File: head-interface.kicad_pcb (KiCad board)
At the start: 2 copper layers, 51.1 x 19.6 mm, 10 parts, among them J1 NOZ, J2 FANS, J3 MOTOR_IN, J4 THERM, J5 HEATER, J6 PART_FAN, J7 FAN, J8 MOTOR

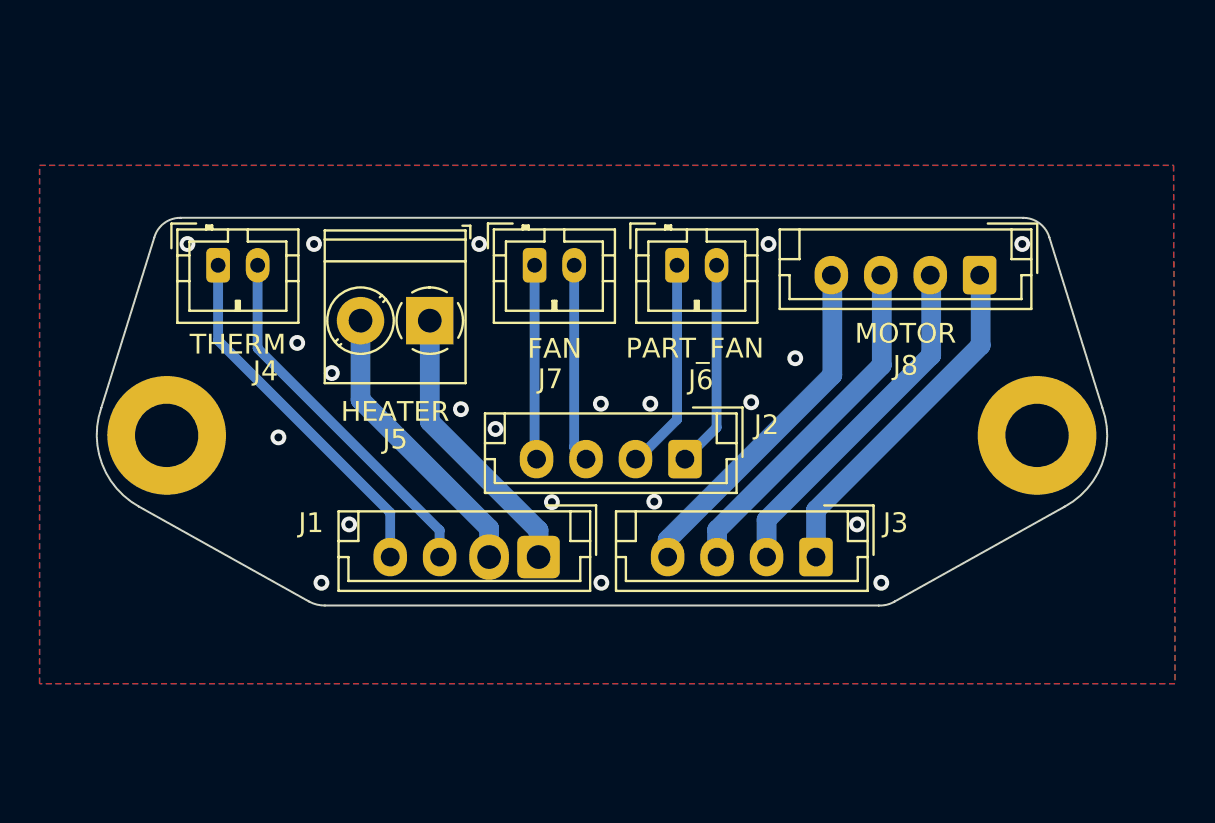
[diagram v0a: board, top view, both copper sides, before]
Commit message: added 2nd part fan connector
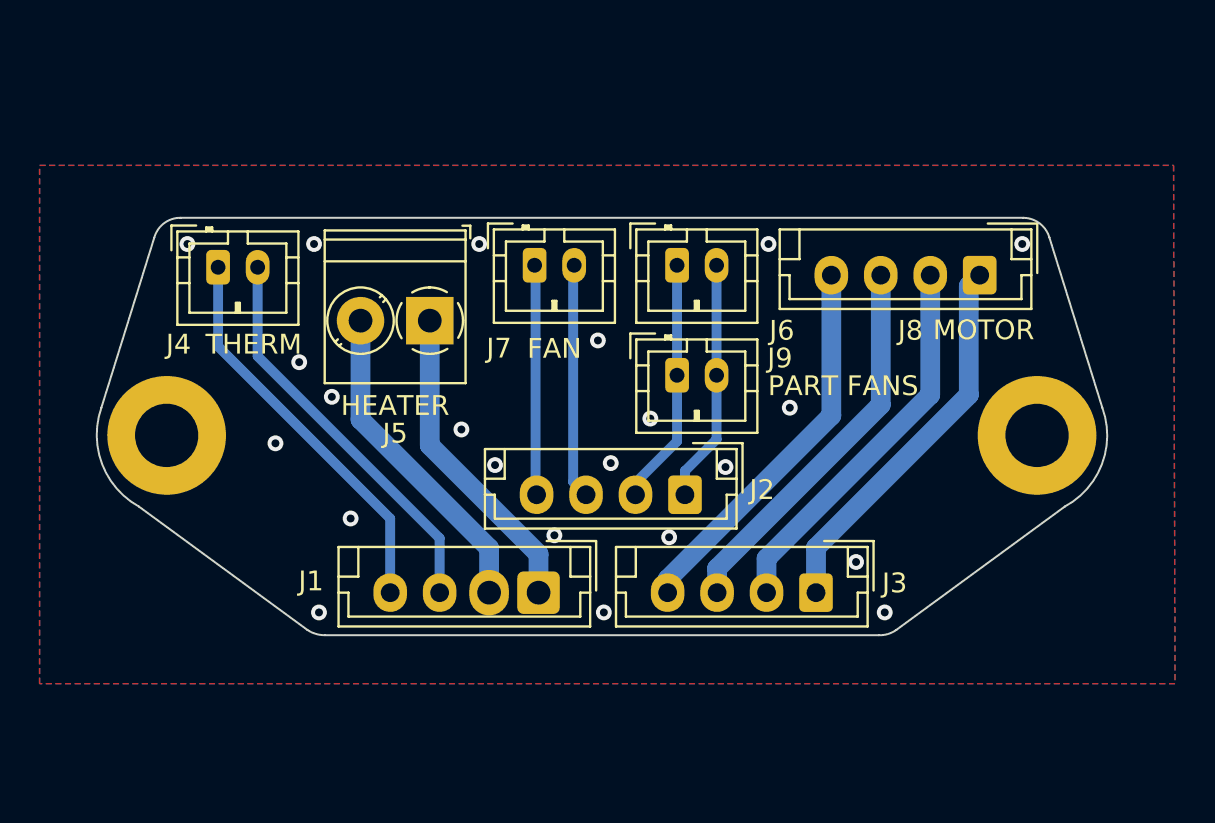
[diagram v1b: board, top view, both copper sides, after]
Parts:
- added J9: PFAN, Connector_JST:JST_PH_B2B-PH-K_1x02_P2.00mm_Vertical, F.Cu at (103.8, 81.9)
- J6: value PART_FAN -> PART FANS
- moved J2 1.80 mm to (104.2, 87.9)
- moved J1 1.80 mm to (96.8, 92.8)
- moved J3 1.80 mm to (110.8, 92.8)
- moved J4 0.10 mm to (80.6, 76.4)
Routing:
- net Net-(J2-Pad3): track 10.0 -> 11.9 mm
- net Net-(J2-Pad1): track 10.5 -> 12.3 mm
- net Net-(J2-Pad4): track 9.84 -> 11.6 mm
- net Net-(J1-Pad2): track 14.6 -> 16.4 mm
- net Net-(J1-Pad1): track 14.2 -> 16.0 mm
- net Net-(J3-Pad4): track 17.7 -> 19.5 mm
- net Net-(J3-Pad3): track 17.7 -> 19.5 mm
- net Net-(J3-Pad2): track 17.7 -> 19.5 mm
- net Net-(J3-Pad1): track 17.7 -> 19.5 mm
- net Net-(J2-Pad2): track 10.7 -> 12.5 mm
- net Net-(J1-Pad3): track 18.6 -> 20.3 mm
- net Net-(J1-Pad4): track 18.4 -> 20.1 mm
- net GND: vias 21 -> 22
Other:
- board size 51.1 x 19.6 mm -> 51.1 x 21.1 mm

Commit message: 'final' tweaks :-)
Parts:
- added ?: , , F.Cu at (100.0, 100.0)
- added ?: , , F.Cu at (100.0, 67.4)
- moved J4 1.15 mm to (80.7, 75.2)
- moved H1 1.15 mm to (78.0, 83.8)
- moved H2 1.15 mm to (122.0, 83.8)
- moved J2 1.15 mm to (104.2, 86.8)
- moved J9 1.15 mm to (103.8, 80.7)
- moved J7 1.15 mm to (96.7, 75.2)
- moved J8 1.15 mm to (119.2, 75.7)
- moved J1 1.15 mm to (96.8, 91.7)
- moved J3 1.15 mm to (110.9, 91.7)
- moved J5 1.15 mm to (91.3, 78.0)
- moved J6 1.15 mm to (103.8, 75.2)
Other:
- board text added: "(0,-32.6) X-CENTER FLIP DOWEL"
- board text removed: "(0,-20) X-CENTER FLIP DOWEL"
